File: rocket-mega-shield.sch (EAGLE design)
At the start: 70 parts, among them J1 1X2-3.5MM, J2 1X2-3.5MM

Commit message: working on revision 2, not done yet
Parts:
- removed 55GACCEL: AD22286-R2, kurt:AD22285-R2
- removed 5VREG: NCP1117DT50G, kurt:NCP1117DT50G
- removed ANALOGV: AYZ0202, SparkFun-Electromechanical:AYZ0202
- removed C5: 10uF, adafruit:C-USC1206
- removed C6: 0.1uF, adafruit:C-USC1206
- removed PWRMUX: TPS2111APWR, kurt:TPS2111A
- removed R9: 3.3k, adafruit:R-US_R1206
- added 200GACCEL: ADXL377, zortness:ADXL377
- added C19, C20, C26: 0.01uF, adafruit:C-USC1206
- added D1: (no value), SparkFun-DiscreteSemi:DIODESMA-ALT
- added FIRST, FOURTH, SECOND, THIRD: MOSFET-NCHANNELSI7112DN, SparkFun-DiscreteSemi:MOSFET-NCHANNELSI7820DN
- added PYRO: 1X6TERMINALBLOCK, zortness:1X6TERMINALBLOCK
- C1: value 10uF -> 100uF
- C4: value 0.1uF -> 100uF
- R1: value 400 -> 10k
- R6, R8: value 1.7k -> 10k
- R7: value 3.3k -> 10k
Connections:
- removed net 5VOUT: 5VREG.OUT, C5.2, C6.1, PWRMUX.D1, PWRMUX.IN1
- removed net BATT_RAW: 5VREG.IN, C1.1, C24.+, C25.+, EXTBATT.2, RELAY1.T1, RELAY2.T1
- removed net VCC5: 3.3VREG.IN, 55GACCEL.VDD@1, 55GACCEL.VDD@2, 55GACCEL.VDD@3, C2.1, C7.1, PWRMUX.OUT
- new net N$1: D1.A, EXTBATT.2
- new net N$24: FOURTH.D, PYRO.6
- new net VIN: 3.3VREG.IN, C2.1, C24.+, C25.+, D1.C, MEGA.VIN, PYRO.1, PYRO.2, RELAY1.T1, RELAY2.T1
- net GND: now also 200GACCEL.GND@1, 200GACCEL.GND@2, C19.2, C20.2, C26.2, FIRST.S, FOURTH.S, SECOND.S, THIRD.S; no longer 55GACCEL.GND, 5VREG.GND, C5.1, C6.2, PWRMUX.D0, PWRMUX.GND, PWRMUX.VSNS, R1.1, R6.2, R7.2, R8.1, R9.1
- net MEGA5V: no longer C4.1, PWRMUX.IN2
- net MEGAA0: now also 200GACCEL.X, C19.1; no longer ANALOGV.1, R6.1, R7.1
- net MEGAA1: now also 200GACCEL.Y, C20.1; no longer ANALOGV.4, R8.2, R9.2
- net MEGAA2: now also 200GACCEL.Z, C26.1; no longer ANALOGV.3
- net MEGAA3: no longer ANALOGV.6
- net N$3: now also FIRST.D, PYRO.3; no longer 55GACCEL.YOUT, ANALOGV.5
- net N$4: now also PYRO.4, SECOND.D; no longer PWRMUX.ILIM, R1.2
- net N$9: now also PYRO.5, THIRD.D; no longer 55GACCEL.XOUT, ANALOGV.2
- net VCC3: now also 200GACCEL.VS@1, 200GACCEL.VS@2, C1.1, C4.1, C7.1
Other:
- note added: "200G Analog Accelerometer"
- note added: "Rocket Mega R2"
- note removed: "55G Analog Accelerometer with output scale switch"
- moved on the sheet: 3.3VREG, C1, C2, C3, C4, C7, PWR, R1, R14, R6, R7, R8

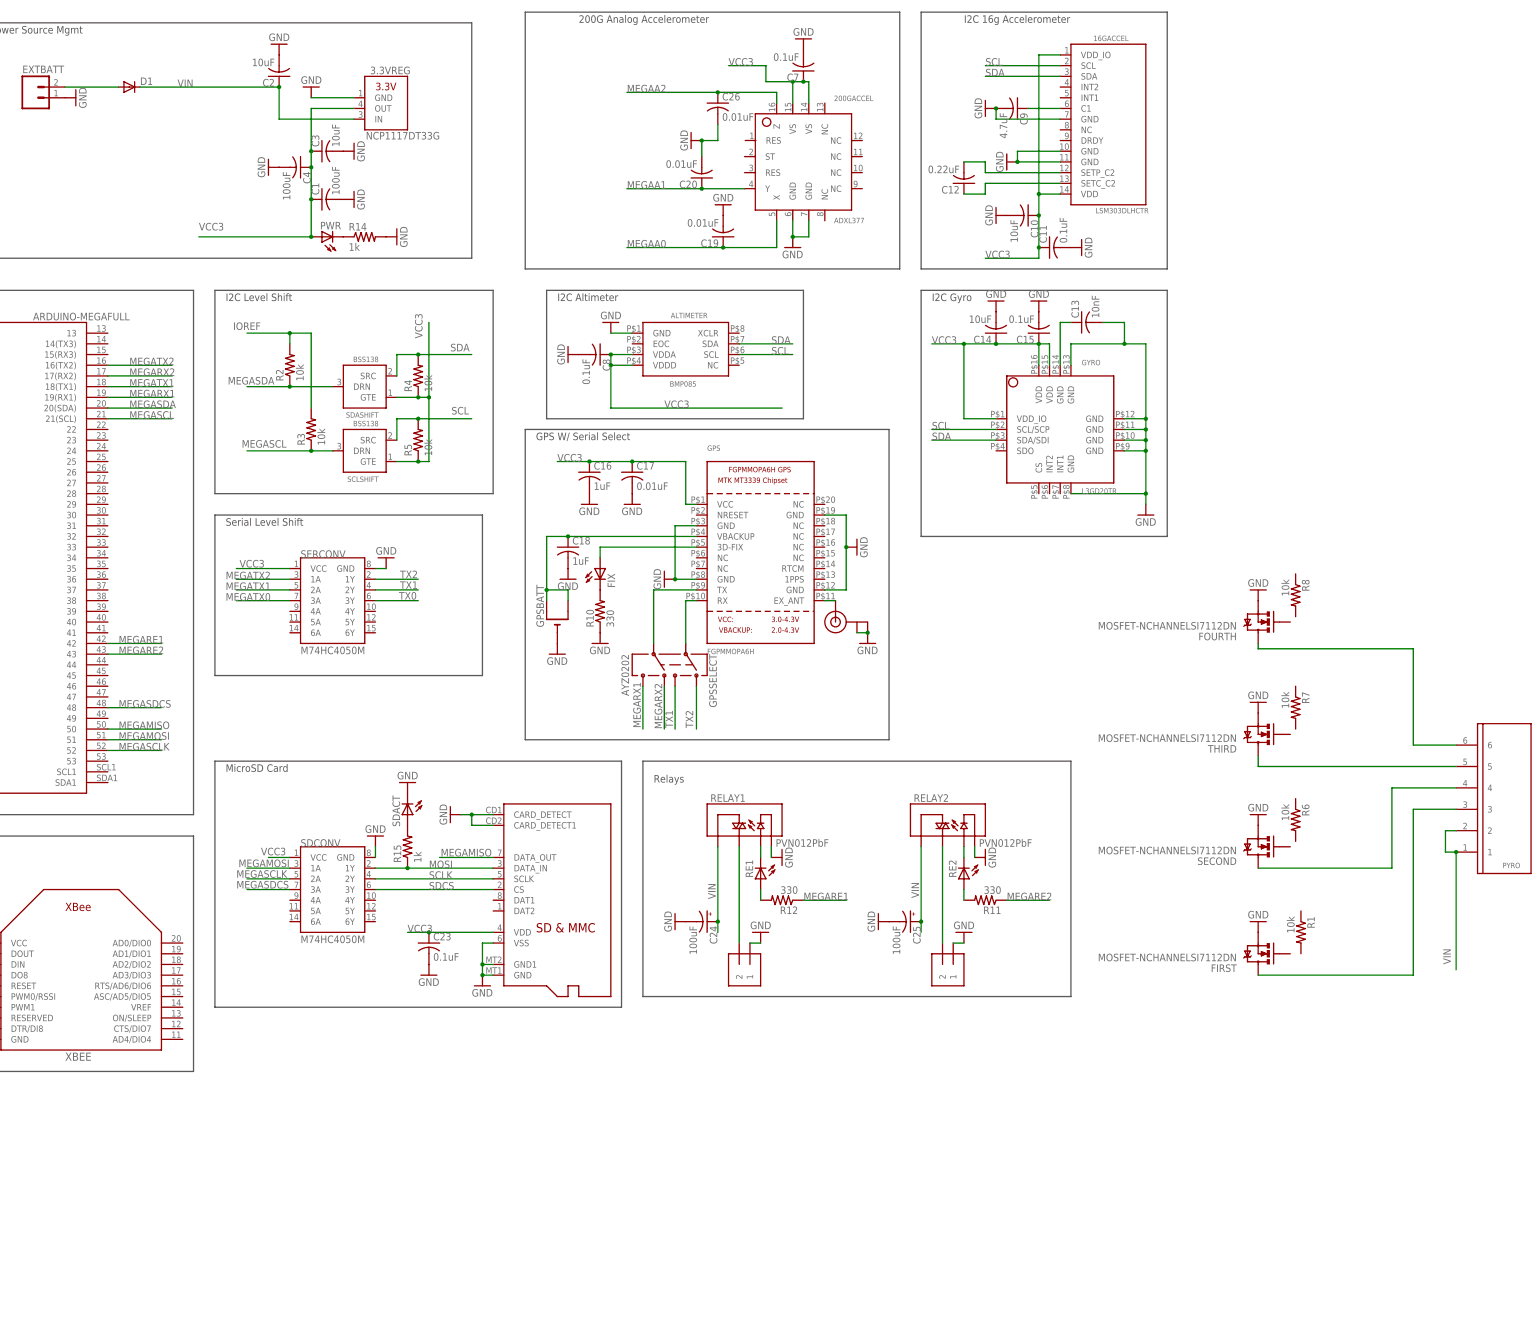
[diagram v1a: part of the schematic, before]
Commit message: initial schematic with mosfets and continuity checking
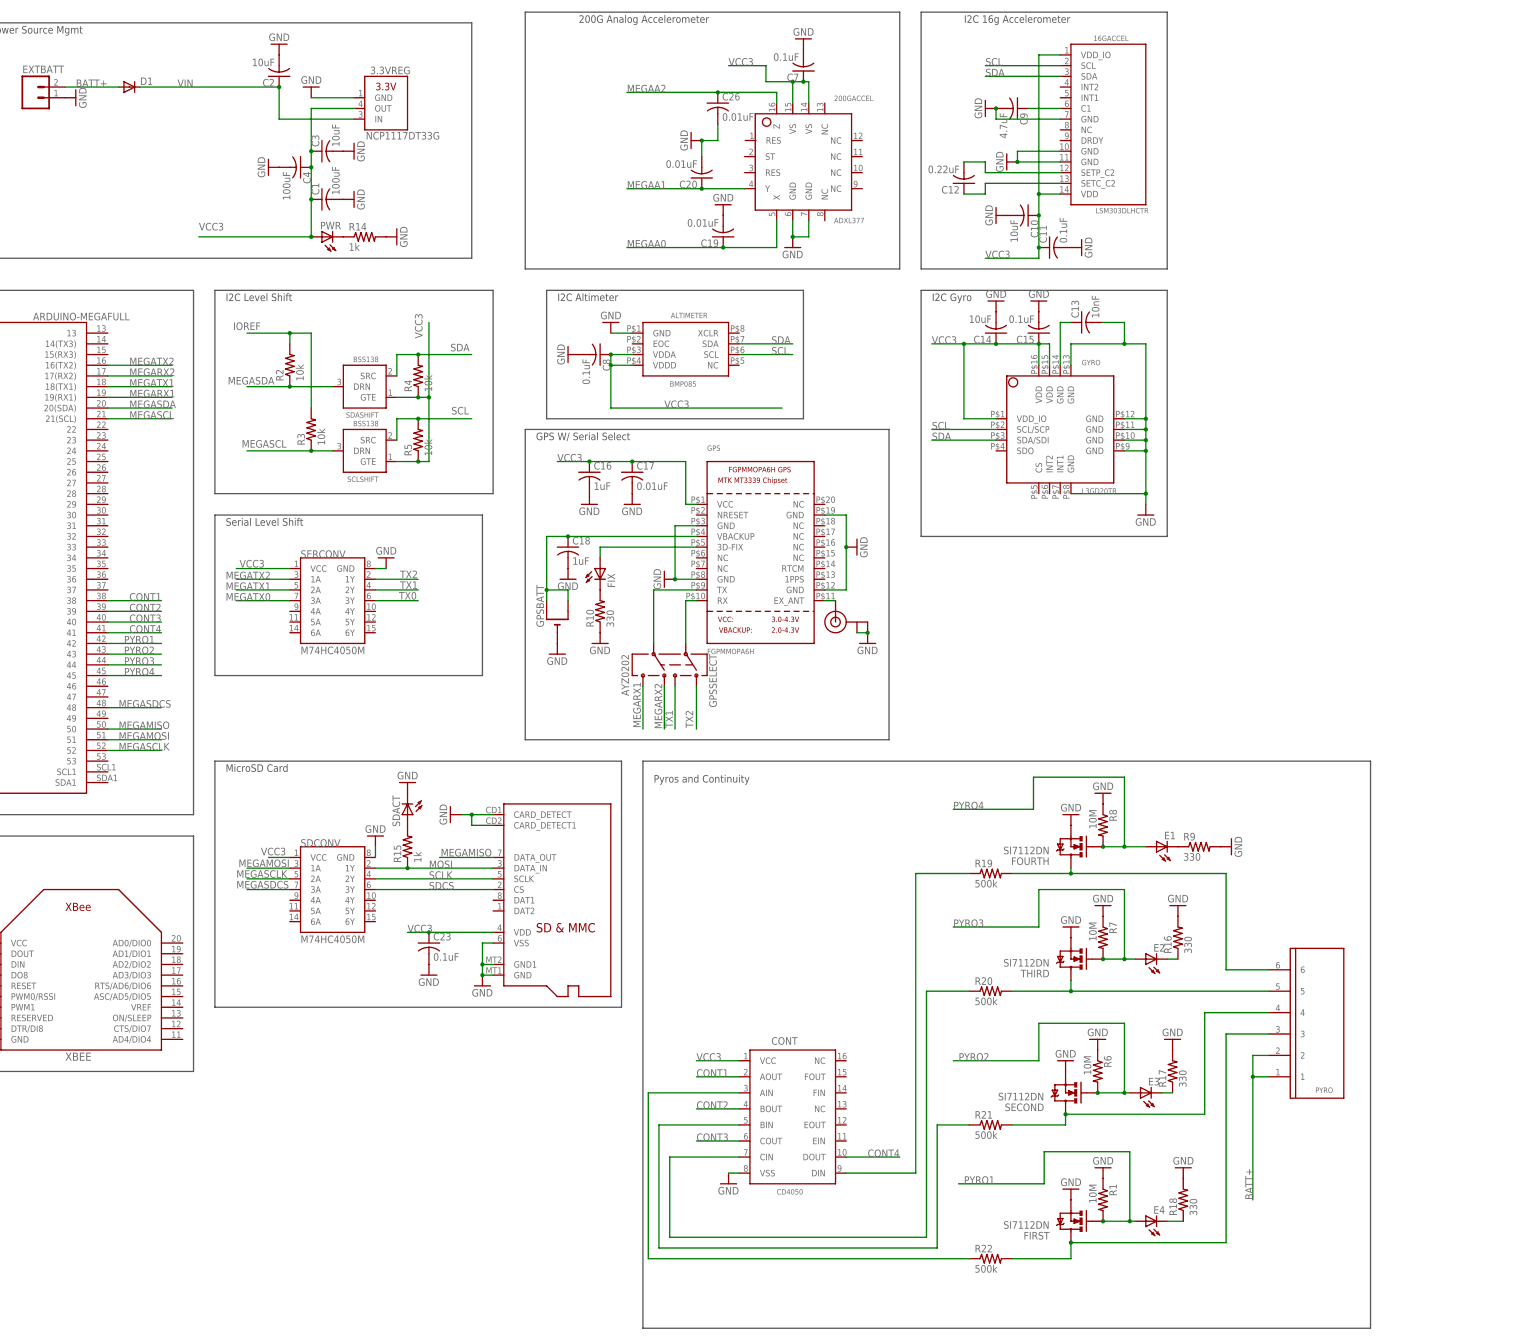
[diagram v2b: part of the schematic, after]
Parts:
- removed C24, C25: 100uF, SparkFun-Capacitors:CAP_POLPTH1
- removed J1, J2: 1X2-3.5MM, adafruit:1X2-3.5MM
- removed R11, R12: 330, adafruit:R-US_R1206
- removed RE1, RE2: (no value), SparkFun-LED:LED1206
- removed RELAY1, RELAY2: PVN012PbF, kurt:RELAY_SOLIDSTATE
- added CONT: CD4050, zortness:CD4050
- added E1, E2, E3, E4: (no value), SparkFun-LED:LED1206
- added R16, R17, R18, R9: 330, adafruit:R-US_R1206
- added R19, R20, R21, R22: 500k, adafruit:R-US_R1206
- FIRST, FOURTH, SECOND, THIRD: value MOSFET-NCHANNELSI7112DN -> SI7112DN
- R1, R6, R7, R8: value 10k -> 10M
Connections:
- removed net MEGARE1: MEGA.42, R12.1
- removed net MEGARE2: MEGA.43, R11.1
- removed net N$1: D1.A, EXTBATT.2
- removed net N$19: RE2.C, RELAY2.+
- removed net N$2: RE1.C, RELAY1.+
- removed net N$20: R11.2, RE2.A
- removed net N$23: R12.2, RE1.A
- removed net R1OUT: J1.2, RELAY1.T2
- removed net R2OUT: J2.2, RELAY2.T2
- new net BATT+: D1.A, EXTBATT.2, PYRO.1, PYRO.2
- new net CONT1: CONT.AOUT, MEGA.38
- new net CONT2: CONT.BOUT, MEGA.39
- new net CONT3: CONT.COUT, MEGA.40
- new net CONT4: CONT.DOUT, MEGA.41
- new net N$29: E1.C, R9.1
- new net N$30: E2.C, R16.1
- new net N$31: E3.C, R17.1
- new net N$32: E4.C, R18.1
- new net N$33: CONT.DIN, R19.1
- new net N$34: CONT.CIN, R20.1
- new net N$35: CONT.BIN, R21.1
- new net N$36: CONT.AIN, R22.1
- new net PYRO1: E4.A, FIRST.G, MEGA.42, R1.2
- new net PYRO2: E3.A, MEGA.43, R6.2, SECOND.G
- new net PYRO3: E2.A, MEGA.44, R7.2, THIRD.G
- new net PYRO4: E1.A, FOURTH.G, MEGA.45, R8.2
- net GND: now also CONT.VSS, R1.1, R16.2, R17.2, R18.2, R6.1, R7.1, R8.1, R9.2; no longer C24.-, C25.-, J1.1, J2.1, RELAY1.-, RELAY2.-
- net N$24: now also R19.2
- net N$3: now also R22.2
- net N$4: now also R21.2
- net N$9: now also R20.2
- net VCC3: now also CONT.VCC
- net VIN: no longer C24.+, C25.+, PYRO.1, PYRO.2, RELAY1.T1, RELAY2.T1
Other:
- note added: "Pyros and Continuity"
- note removed: "Relays"
- moved on the sheet: FIRST, FOURTH, PYRO, R1, R6, R7, R8, SECOND, THIRD

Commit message: working on layout for rev2
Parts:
- removed GPSSELECT: AYZ0202, SparkFun-Electromechanical:AYZ0202
- removed SDCONV: M74HC4050M, SparkFun-DigitalIC:HEX_CONVERTER
- C4: value 100uF -> 220uF; device adafruit:C-USC1206 -> adafruit:C-USC1210
- renumbered SERCONV to CONV
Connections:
- removed net MEGAA3: MEGA.A3
- removed net N$11: GPS.TX, GPSSELECT.5
- removed net N$12: GPS.RX, GPSSELECT.2
- removed net TX2: CONV.1Y, GPSSELECT.1
- net GND: no longer SDCONV.GND
- net MEGAMOSI: now also CONV.3A; no longer SDCONV.1A
- net MEGARX1: now also GPS.TX; no longer GPSSELECT.6, XBEESELECT.4
- net MEGARX2: no longer GPSSELECT.4
- net MEGASCLK: now also CONV.4A; no longer SDCONV.2A
- net MEGASDCS: now also CONV.5A; no longer SDCONV.3A
- net MEGATX0: now also CONV.1A; no longer CONV.3A
- net MEGATX2: no longer CONV.1A
- net MOSI: now also CONV.3Y; no longer SDCONV.1Y
- net N$29: now also E4.C; no longer E1.C
- net N$30: now also E3.C; no longer E2.C
- net N$31: now also E2.C; no longer E3.C
- net N$32: now also E1.C; no longer E4.C
- net PYRO1: now also E1.A; no longer E4.A
- net PYRO2: now also E2.A; no longer E3.A
- net PYRO3: now also E3.A; no longer E2.A
- net PYRO4: now also E4.A; no longer E1.A
- net SCLK: now also CONV.4Y; no longer SDCONV.2Y
- net SDCS: now also CONV.5Y; no longer SDCONV.3Y
- net TX0: now also CONV.1Y; no longer CONV.3Y
- net TX1: now also GPS.RX; no longer GPSSELECT.3, XBEESELECT.1
- net VCC3: no longer SDCONV.VCC
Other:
- note added: "Unidirectional Logic Level Shifter"
- note removed: "Serial Level Shift"
- moved on the sheet: E1, E2, E3, E4

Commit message: mostly done with schematic and layout... still need to add fuse and clean up labeling
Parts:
- removed C18: 1uF, adafruit:C-USC1206
- removed CONT: CD4050, zortness:CD4050
- removed GPSBATT: (no value), adafruit:CR1220SMT
- removed R1, R6, R7, R8: 10M, adafruit:R-US_R1206
- removed R10, R16, R17, R18, R9: 330, adafruit:R-US_R1206
- removed R13, R14, R15: 1k, adafruit:R-US_R1206
- removed R19, R20, R21, R22: 500k, adafruit:R-US_R1206
- removed R2, R3, R4, R5: 10k, adafruit:R-US_R1206
- added RA1, RA5: 330, zortness:RESISTOR_CRA06S08
- added RA2, RA6: 10k, zortness:RESISTOR_CRA06S08
- added RA3: 620k, zortness:RESISTOR_CRA06S08
- added RA4: 110k, zortness:RESISTOR_CRA06S08
- C2: value 10uF -> 100uF16V
- D1: value (none) -> STTH102A
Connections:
- removed net CONT1: CONT.AOUT, MEGA.38
- removed net CONT2: CONT.BOUT, MEGA.39
- removed net CONT3: CONT.COUT, MEGA.40
- removed net CONT4: CONT.DOUT, MEGA.41
- removed net N$13: C18.1, GPS.VBACKUP, GPSBATT.+, GPSBATT.+1
- removed net N$14: FIX.A, GPS.3D-FIX
- removed net N$15: FIX.C, R10.2
- removed net N$26: R15.2, SDACT.A
- removed net N$29: E4.C, R9.1
- removed net N$30: E3.C, R16.1
- removed net N$31: E2.C, R17.1
- removed net N$32: E1.C, R18.1
- removed net N$33: CONT.DIN, R19.1
- removed net N$34: CONT.CIN, R20.1
- removed net N$35: CONT.BIN, R21.1
- removed net N$36: CONT.AIN, R22.1
- removed net N$9: PYRO.5, R20.2, THIRD.D
- new net GPSFIX: GPS.3D-FIX, RA1.A1
- new net MEGAA3: MEGA.A3, RA3.D1, RA4.D2
- new net MEGAA4: MEGA.A4, RA3.C1, RA4.C2
- new net MEGAA5: MEGA.A5, RA3.B1, RA4.B2
- new net MEGAA6: MEGA.A6, RA3.A1, RA4.A2
- new net N$1: PWR.A, RA1.D2
- new net N$11: RA1.B2, RSSI.A
- new net N$12: FIX.A, RA1.A2
- new net N$19: E1.A, RA5.A2
- new net N$2: RA1.C2, SDACT.A
- new net N$25: PYRO.5, RA3.B2, THIRD.D
- new net TX2: CONV.3Y, GPS.RX
- new net XRSSI: RA1.B1, XBEE.PWM0/RSSI
- net GND: now also E1.C, E2.C, E3.C, E4.C, FIX.C, PWR.C, RA4.A1, RA4.B1, RA4.C1, RA4.D1, RA6.A2, RA6.B2, RA6.C2, RA6.D2; no longer C18.2, CONT.VSS, GPSBATT.-, R1.1, R10.1, R14.2, R16.2, R17.2, R18.2, R6.1, R7.1, R8.1, R9.2
- net IOREF: now also RA2.A1, RA2.B1; no longer R2.2, R3.2
- net MEGAMOSI: now also CONV.4A; no longer CONV.3A
- net MEGARX1: now also XBEESELECT.4; no longer GPS.TX
- net MEGARX2: now also GPS.TX
- net MEGASCL: now also RA2.B2; no longer R3.1
- net MEGASCLK: now also CONV.5A; no longer CONV.4A
- net MEGASDA: now also RA2.A2; no longer R2.1
- net MEGASDCS: now also CONV.6A; no longer CONV.5A
- net MEGATX2: now also CONV.3A
- net MOSI: now also CONV.4Y, RA1.C1; no longer CONV.3Y, R15.1
- net N$16: now also E4.A, RA5.D2; no longer PWR.C, R14.1
- net N$17: now also E3.A, RA5.C2; no longer R13.2, XBEE.PWM0/RSSI
- net N$18: now also E2.A, RA5.B2; no longer R13.1, RSSI.A
- net N$24: now also RA3.A2; no longer R19.2
- net N$3: now also RA3.D2; no longer R22.2
- net N$4: now also RA3.C2; no longer R21.2
- net PYRO1: now also RA5.A1, RA6.A1; no longer E1.A, R1.2
- net PYRO2: now also RA5.B1, RA6.B1; no longer E2.A, R6.2
- net PYRO3: now also RA5.C1, RA6.C1; no longer E3.A, R7.2
- net PYRO4: now also RA5.D1, RA6.D1; no longer E4.A, R8.2
- net SCL: now also RA2.C2; no longer R5.2
- net SCLK: now also CONV.5Y; no longer CONV.4Y
- net SDA: now also RA2.D2; no longer R4.2
- net SDCS: now also CONV.6Y; no longer CONV.5Y
- net TX1: now also XBEESELECT.1; no longer GPS.RX
- net VCC3: now also RA1.D1, RA2.C1, RA2.D1; no longer CONT.VCC, PWR.A, R4.1, R5.1
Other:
- note added: "200G Accel"
- note added: "Continuity"
- note added: "GPS"
- note added: "I2C 16g Accel / Mag"
- note added: "LED Bank 1"
- note added: "XBee TX0/RX0 or GPS Selector"
- note removed: "GPS W/ Serial Select"
- note removed: "I2C 16g Accelerometer"
- note removed: "XBee w/ Serial Select"
- moved on the sheet: 16GACCEL, 200GACCEL, 3.3VREG, ALTIMETER, C1, C10, C11, C12, C13, C14, C15, C16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
